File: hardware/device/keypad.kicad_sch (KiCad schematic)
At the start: 76 parts, among them SW1 TRIG1, SW10 TRIG10, SW11 TRIG11, SW12 TRIG12, SW13 TRIG13, SW14 TRIG14, SW15 TRIG15, SW16 TRIG16, SW17 WHEEL_BTN, SW18 HELP, SW19 LEFT_BTN, SW2 TRIG2, SW20 RIGHT_BTN, SW3 TRIG3, SW4 TRIG4, SW5 TRIG5, SW6 TRIG6, SW7 TRIG7, SW8 TRIG8, SW9 TRIG9, U25 TCA8418RTWR

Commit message: feat: start routing keyswitch pads
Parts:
- D1, D10, D11, D12, D13, D14, D15, D16, D2, D22, D23, D24, D25, D26, D27, D28, D29, D3, D30, D31, D32, D33, D34, D35, D36, D37, D4, D5, D6, D7, D8, D9: footprint Diode_SMD:D_0603_1608Metric_Pad1.05x0.95mm_HandSolder -> Diode_SMD:D_0402_1005Metric
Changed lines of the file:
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@@
 			)
 		)
-		(property "Footprint" "Diode_SMD:D_0603_1608Metric_Pad1.05x0.95mm_HandSolder"
+		(property "Footprint" "Diode_SMD:D_0402_1005Metric"
 			(at 179.07 35.56 0)
 			(effects
@@
 			)
 		)
-		(property "Footprint" "Diode_SMD:D_0603_1608Metric_Pad1.05x0.95mm_HandSolder"
+		(property "Footprint" "Diode_SMD:D_0402_1005Metric"
 			(at 224.79 127 0)
 			(effects
@@
 			)
 		)
-		(property "Footprint" "Diode_SMD:D_0603_1608Metric_Pad1.05x0.95mm_HandSolder"
+		(property "Footprint" "Diode_SMD:D_0402_1005Metric"
 			(at 152.4 127 0)
 			(effects
@@
 			)
 		)
-		(property "Footprint" "Diode_SMD:D_0603_1608Metric_Pad1.05x0.95mm_HandSolder"
+		(property "Footprint" "Diode_SMD:D_0402_1005Metric"
 			(at 204.47 50.8 0)
 			(effects
@@
 			)
 		)
-		(property "Footprint" "Diode_SMD:D_0603_1608Metric_Pad1.05x0.95mm_HandSolder"
+		(property "Footprint" "Diode_SMD:D_0402_1005Metric"
 			(at 176.53 111.76 0)
 			(effects
@@
 			)
 		)
-		(property "Footprint" "Diode_SMD:D_0603_1608Metric_Pad1.05x0.95mm_HandSolder"
+		(property "Footprint" "Diode_SMD:D_0402_1005Metric"
 			(at 229.87 66.04 0)
 			(effects
@@
 			)
 		)
-		(property "Footprint" "Diode_SMD:D_0603_1608Metric_Pad1.05x0.95mm_HandSolder"
+		(property "Footprint" "Diode_SMD:D_0402_1005Metric"
 			(at 153.67 35.56 0)
 			(effects
@@
 			)
 		)
-		(property "Footprint" "Diode_SMD:D_0603_1608Metric_Pad1.05x0.95mm_HandSolder"
+		(property "Footprint" "Diode_SMD:D_0402_1005Metric"
 			(at 200.66 142.24 0)
 			(effects
@@
 			)
 		)
-		(property "Footprint" "Diode_SMD:D_0603_1608Metric_Pad1.05x0.95mm_HandSolder"
+		(property "Footprint" "Diode_SMD:D_0402_1005Metric"
 			(at 200.66 111.76 0)
 			(effects
@@
 			)
 		)
-		(property "Footprint" "Diode_SMD:D_0603_1608Metric_Pad1.05x0.95mm_HandSolder"
+		(property "Footprint" "Diode_SMD:D_0402_1005Metric"
 			(at 179.07 50.8 0)
 			(effects
@@
 			)
 		)
-		(property "Footprint" "Diode_SMD:D_0603_1608Metric_Pad1.05x0.95mm_HandSolder"
+		(property "Footprint" "Diode_SMD:D_0402_1005Metric"
 			(at 179.07 81.28 0)
 			(effects
@@
 			)
 		)
-		(property "Footprint" "Diode_SMD:D_0603_1608Metric_Pad1.05x0.95mm_HandSolder"
+		(property "Footprint" "Diode_SMD:D_0402_1005Metric"
 			(at 153.67 81.28 0)
 			(effects
@@
 			)
 		)
-		(property "Footprint" "Diode_SMD:D_0603_1608Metric_Pad1.05x0.95mm_HandSolder"
+		(property "Footprint" "Diode_SMD:D_0402_1005Metric"
 			(at 224.79 157.48 0)
 			(effects
@@
 			)
 		)
-		(property "Footprint" "Diode_SMD:D_0603_1608Metric_Pad1.05x0.95mm_HandSolder"
+		(property "Footprint" "Diode_SMD:D_0402_1005Metric"
 			(at 224.79 142.24 0)
 			(effects
@@
 			)
 		)
-		(property "Footprint" "Diode_SMD:D_0603_1608Metric_Pad1.05x0.95mm_HandSolder"
+		(property "Footprint" "Diode_SMD:D_0402_1005Metric"
 			(at 152.4 142.24 0)
 			(effects
@@
 			)
 		)
-		(property "Footprint" "Diode_SMD:D_0603_1608Metric_Pad1.05x0.95mm_HandSolder"
+		(property "Footprint" "Diode_SMD:D_0402_1005Metric"
 			(at 204.47 35.56 0)
 			(effects
@@
 			)
 		)
-		(property "Footprint" "Diode_SMD:D_0603_1608Metric_Pad1.05x0.95mm_HandSolder"
+		(property "Footprint" "Diode_SMD:D_0402_1005Metric"
 			(at 152.4 111.76 0)
 			(effects
@@
 			)
 		)
-		(property "Footprint" "Diode_SMD:D_0603_1608Metric_Pad1.05x0.95mm_HandSolder"
+		(property "Footprint" "Diode_SMD:D_0402_1005Metric"
 			(at 152.4 157.48 0)
 			(effects
@@
 			)
 		)
-		(property "Footprint" "Diode_SMD:D_0603_1608Metric_Pad1.05x0.95mm_HandSolder"
+		(property "Footprint" "Diode_SMD:D_0402_1005Metric"
 			(at 204.47 66.04 0)
 			(effects
@@
 			)
 		)
-		(property "Footprint" "Diode_SMD:D_0603_1608Metric_Pad1.05x0.95mm_HandSolder"
+		(property "Footprint" "Diode_SMD:D_0402_1005Metric"
 			(at 204.47 81.28 0)
 			(effects
@@
 			)
 		)
-		(property "Footprint" "Diode_SMD:D_0603_1608Metric_Pad1.05x0.95mm_HandSolder"
+		(property "Footprint" "Diode_SMD:D_0402_1005Metric"
 			(at 200.66 127 0)
 			(effects
@@
 			)
 		)
-		(property "Footprint" "Diode_SMD:D_0603_1608Metric_Pad1.05x0.95mm_HandSolder"
+		(property "Footprint" "Diode_SMD:D_0402_1005Metric"
 			(at 229.87 50.8 0)
 			(effects
@@
 			)
 		)
-		(property "Footprint" "Diode_SMD:D_0603_1608Metric_Pad1.05x0.95mm_HandSolder"
+		(property "Footprint" "Diode_SMD:D_0402_1005Metric"
 			(at 229.87 35.56 0)
 			(effects
@@
 			)
 		)
-		(property "Footprint" "Diode_SMD:D_0603_1608Metric_Pad1.05x0.95mm_HandSolder"
+		(property "Footprint" "Diode_SMD:D_0402_1005Metric"
 			(at 224.79 111.76 0)
 			(effects
@@
 			)
 		)
-		(property "Footprint" "Diode_SMD:D_0603_1608Metric_Pad1.05x0.95mm_HandSolder"
+		(property "Footprint" "Diode_SMD:D_0402_1005Metric"
 			(at 153.67 50.8 0)
 			(effects
@@
 			)
 		)
-		(property "Footprint" "Diode_SMD:D_0603_1608Metric_Pad1.05x0.95mm_HandSolder"
+		(property "Footprint" "Diode_SMD:D_0402_1005Metric"
 			(at 153.67 66.04 0)
 			(effects
@@
 			)
 		)
-		(property "Footprint" "Diode_SMD:D_0603_1608Metric_Pad1.05x0.95mm_HandSolder"
+		(property "Footprint" "Diode_SMD:D_0402_1005Metric"
 			(at 176.53 157.48 0)
 			(effects
@@
 			)
 		)
-		(property "Footprint" "Diode_SMD:D_0603_1608Metric_Pad1.05x0.95mm_HandSolder"
+		(property "Footprint" "Diode_SMD:D_0402_1005Metric"
 			(at 229.87 81.28 0)
 			(effects
@@
 			)
 		)
-		(property "Footprint" "Diode_SMD:D_0603_1608Metric_Pad1.05x0.95mm_HandSolder"
+		(property "Footprint" "Diode_SMD:D_0402_1005Metric"
 			(at 200.66 157.48 0)
 			(effects
@@
 			)
 		)
-		(property "Footprint" "Diode_SMD:D_0603_1608Metric_Pad1.05x0.95mm_HandSolder"
+		(property "Footprint" "Diode_SMD:D_0402_1005Metric"
 			(at 176.53 127 0)
 			(effects
@@
 			)
 		)
-		(property "Footprint" "Diode_SMD:D_0603_1608Metric_Pad1.05x0.95mm_HandSolder"
+		(property "Footprint" "Diode_SMD:D_0402_1005Metric"
 			(at 176.53 142.24 0)
 			(effects
@@
 			)
 		)
-		(property "Footprint" "Diode_SMD:D_0603_1608Metric_Pad1.05x0.95mm_HandSolder"
+		(property "Footprint" "Diode_SMD:D_0402_1005Metric"
 			(at 179.07 66.04 0)
 			(effects

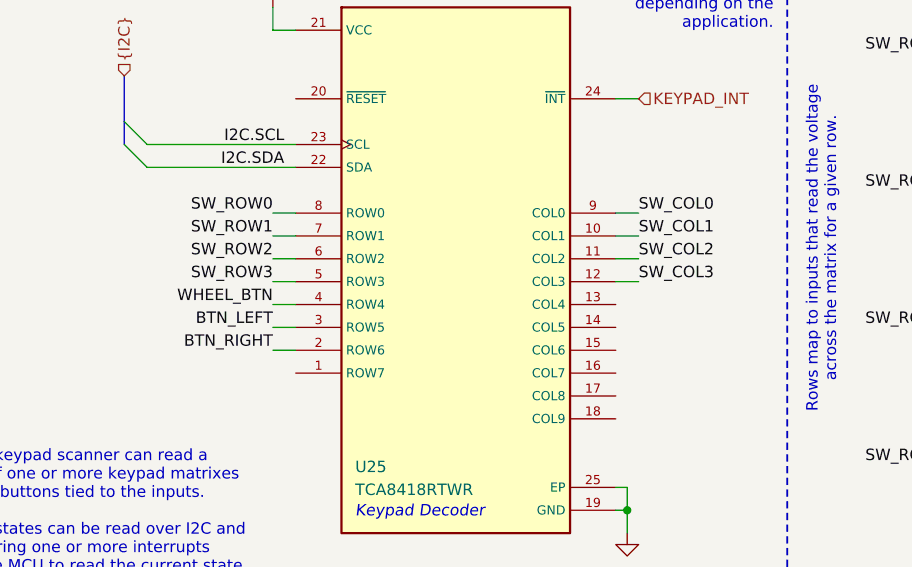
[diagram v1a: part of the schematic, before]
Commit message: feat: keypad routing and layout
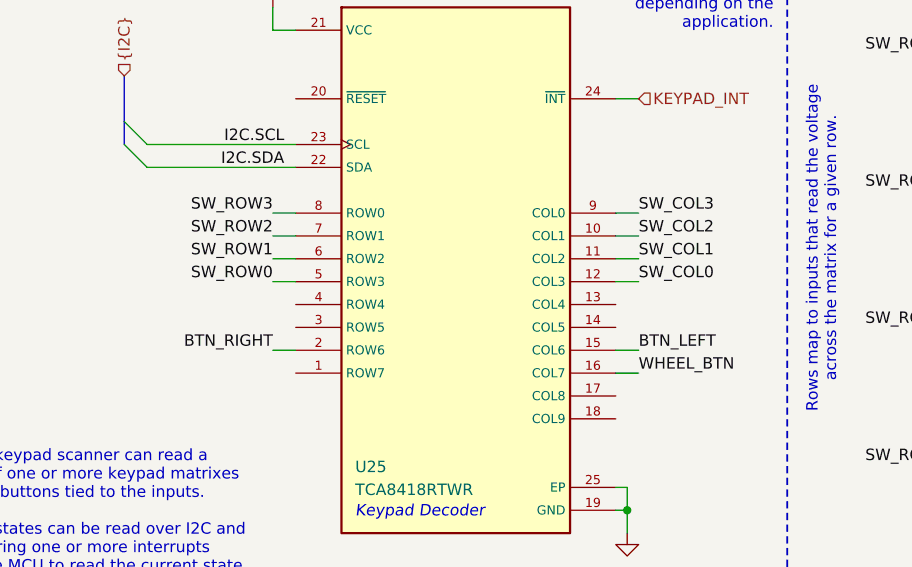
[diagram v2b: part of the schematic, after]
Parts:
- TP1, TP10, TP11, TP12, TP13, TP16, TP17, TP18, TP2, TP3, TP4, TP5, TP6, TP7, TP8, TP9: footprint TestPoint:TestPoint_Pad_D1.5mm -> TestPoint:TestPoint_Pad_D1.0mm
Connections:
- net BTN_LEFT: now also U25.15 (COL6); no longer U25.3 (ROW5)
- net SW_COL0: now also U25.12 (COL3); no longer U25.9 (COL0)
- net SW_COL1: now also U25.11 (COL2); no longer U25.10 (COL1)
- net SW_COL2: now also U25.10 (COL1); no longer U25.11 (COL2)
- net SW_COL3: now also U25.9 (COL0); no longer U25.12 (COL3)
- net SW_ROW0: now also U25.5 (ROW3); no longer U25.8 (ROW0)
- net SW_ROW1: now also U25.6 (ROW2); no longer U25.7 (ROW1)
- net SW_ROW2: now also U25.7 (ROW1); no longer U25.6 (ROW2)
- net SW_ROW3: now also U25.8 (ROW0); no longer U25.5 (ROW3)
- net WHEEL_BTN: now also U25.16 (COL7); no longer U25.4 (ROW4)
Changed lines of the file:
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@@
 	(wire
 		(pts
-			(xy 57.15 55.88) (xy 59.69 55.88)
+			(xy 97.79 63.5) (xy 95.25 63.5)
 		)
 		(stroke
@@
 	(wire
 		(pts
-			(xy 57.15 58.42) (xy 59.69 58.42)
+			(xy 97.79 60.96) (xy 95.25 60.96)
 		)
 		(stroke
@@
 	(wire
 		(pts
-			(xy 57.15 53.34) (xy 59.69 53.34)
+			(xy 57.15 45.72) (xy 59.69 45.72)
 		)
 		(stroke
@@
 	(wire
 		(pts
-			(xy 95.25 53.34) (xy 97.79 53.34)
+			(xy 95.25 45.72) (xy 97.79 45.72)
 		)
 		(stroke
@@
 	(wire
 		(pts
-			(xy 57.15 45.72) (xy 59.69 45.72)
+			(xy 57.15 53.34) (xy 59.69 53.34)
 		)
 		(stroke
@@
 	(wire
 		(pts
-			(xy 57.15 50.8) (xy 59.69 50.8)
+			(xy 57.15 48.26) (xy 59.69 48.26)
 		)
 		(stroke
@@
 	(wire
 		(pts
-			(xy 95.25 45.72) (xy 97.79 45.72)
+			(xy 95.25 53.34) (xy 97.79 53.34)
 		)
 		(stroke
@@
 	(wire
 		(pts
-			(xy 57.15 48.26) (xy 59.69 48.26)
+			(xy 57.15 50.8) (xy 59.69 50.8)
 		)
 		(stroke
@@
 	(wire
 		(pts
-			(xy 95.25 48.26) (xy 97.79 48.26)
+			(xy 95.25 50.8) (xy 97.79 50.8)
 		)
 		(stroke
@@
 	(wire
 		(pts
-			(xy 95.25 50.8) (xy 97.79 50.8)
+			(xy 95.25 48.26) (xy 97.79 48.26)
 		)
 		(stroke
@@
 	)
 	(label "BTN_LEFT"
-		(at 57.15 58.42 180)
+		(at 97.79 60.96 0)
 		(effects
 			(font
@@
 				(thickness 0.1588)
 			)
-			(justify right bottom)
+			(justify left bottom)
 		)
 	)
@@
 	)
 	(label "WHEEL_BTN"
-		(at 57.15 55.88 180)
+		(at 97.79 63.5 0)
 		(effects
 			(font
@@
 				(thickness 0.1588)
 			)
-			(justify right bottom)
+			(justify left bottom)
 		)
 	)
@@
 	)
 	(label "SW_ROW0"
-		(at 57.15 45.72 180)
+		(at 57.15 53.34 180)
 		(effects
 			(font
@@
 	)
 	(label "SW_ROW3"
-		(at 57.15 53.34 180)
+		(at 57.15 45.72 180)
 		(effects
 			(font
@@
 	)
 	(label "SW_COL0"
-		(at 97.79 45.72 0)
+		(at 97.79 53.34 0)
 		(effects
 			(font
@@
 	)
 	(label "SW_COL3"
-		(at 97.79 53.34 0)
+		(at 97.79 45.72 0)
 		(effects
 			(font
@@
 	)
 	(label "SW_COL1"
-		(at 97.79 48.26 0)
+		(at 97.79 50.8 0)
 		(effects
 			(font
@@
 	)
 	(label "SW_ROW1"
-		(at 57.15 48.26 180)
+		(at 57.15 50.8 180)
 		(effects
 			(font
@@
 	)
 	(label "SW_COL2"
-		(at 97.79 50.8 0)
+		(at 97.79 48.26 0)
 		(effects
 			(font
@@
 	)
 	(label "SW_ROW2"
-		(at 57.15 50.8 180)
+		(at 57.15 48.26 180)
 		(effects
 			(font
@@
 			)
 		)
-		(property "Footprint" "TestPoint:TestPoint_Pad_D1.5mm"
+		(property "Footprint" "TestPoint:TestPoint_Pad_D1.0mm"
 			(at 260.35 48.26 0)
 			(effects
@@
 			)
 		)
-		(property "Footprint" "TestPoint:TestPoint_Pad_D1.5mm"
+		(property "Footprint" "TestPoint:TestPoint_Pad_D1.0mm"
 			(at 260.35 67.31 0)
 			(effects
@@
 			)
 		)
-		(property "Footprint" "TestPoint:TestPoint_Pad_D1.5mm"
+		(property "Footprint" "TestPoint:TestPoint_Pad_D1.0mm"
 			(at 265.43 130.81 0)
 			(effects
@@
 			)
 		)
-		(property "Footprint" "TestPoint:TestPoint_Pad_D1.5mm"
+		(property "Footprint" "TestPoint:TestPoint_Pad_D1.0mm"
 			(at 260.35 35.56 0)
 			(effects
@@
 			)
 		)
-		(property "Footprint" "TestPoint:TestPoint_Pad_D1.5mm"
+		(property "Footprint" "TestPoint:TestPoint_Pad_D1.0mm"
 			(at 260.35 54.61 0)
 			(effects
@@
 			)
 		)
-		(property "Footprint" "TestPoint:TestPoint_Pad_D1.5mm"
+		(property "Footprint" "TestPoint:TestPoint_Pad_D1.0mm"
 			(at 260.35 60.96 0)
 			(effects
@@
 			)
 		)
-		(property "Footprint" "TestPoint:TestPoint_Pad_D1.5mm"
+		(property "Footprint" "TestPoint:TestPoint_Pad_D1.0mm"
 			(at 265.43 156.21 0)
 			(effects
@@
 			)
 		)
-		(property "Footprint" "TestPoint:TestPoint_Pad_D1.5mm"
+		(property "Footprint" "TestPoint:TestPoint_Pad_D1.0mm"
 			(at 260.35 73.66 0)
 			(effects
@@
 			)
 		)
-		(property "Footprint" "TestPoint:TestPoint_Pad_D1.5mm"
+		(property "Footprint" "TestPoint:TestPoint_Pad_D1.0mm"
 			(at 260.35 80.01 0)
 			(effects
@@
 			)
 		)
-		(property "Footprint" "TestPoint:TestPoint_Pad_D1.5mm"
+		(property "Footprint" "TestPoint:TestPoint_Pad_D1.0mm"
 			(at 265.43 162.56 0)
 			(effects
@@
 			)
 		)
-		(property "Footprint" "TestPoint:TestPoint_Pad_D1.5mm"
+		(property "Footprint" "TestPoint:TestPoint_Pad_D1.0mm"
 			(at 265.43 118.11 0)
 			(effects
@@
 			)
 		)
-		(property "Footprint" "TestPoint:TestPoint_Pad_D1.5mm"
+		(property "Footprint" "TestPoint:TestPoint_Pad_D1.0mm"
 			(at 265.43 143.51 0)
 			(effects
@@
 			)
 		)
-		(property "Footprint" "TestPoint:TestPoint_Pad_D1.5mm"
+		(property "Footprint" "TestPoint:TestPoint_Pad_D1.0mm"
 			(at 265.43 124.46 0)
 			(effects
@@
 			)
 		)
-		(property "Footprint" "TestPoint:TestPoint_Pad_D1.5mm"
+		(property "Footprint" "TestPoint:TestPoint_Pad_D1.0mm"
 			(at 265.43 137.16 0)
 			(effects
@@
 			)
 		)
-		(property "Footprint" "TestPoint:TestPoint_Pad_D1.5mm"
+		(property "Footprint" "TestPoint:TestPoint_Pad_D1.0mm"
 			(at 265.43 149.86 0)
 			(effects
@@
 			)
 		)
-		(property "Footprint" "TestPoint:TestPoint_Pad_D1.5mm"
+		(property "Footprint" "TestPoint:TestPoint_Pad_D1.0mm"
 			(at 260.35 41.91 0)
 			(effects
